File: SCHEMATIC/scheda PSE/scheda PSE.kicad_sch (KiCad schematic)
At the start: 4 parts

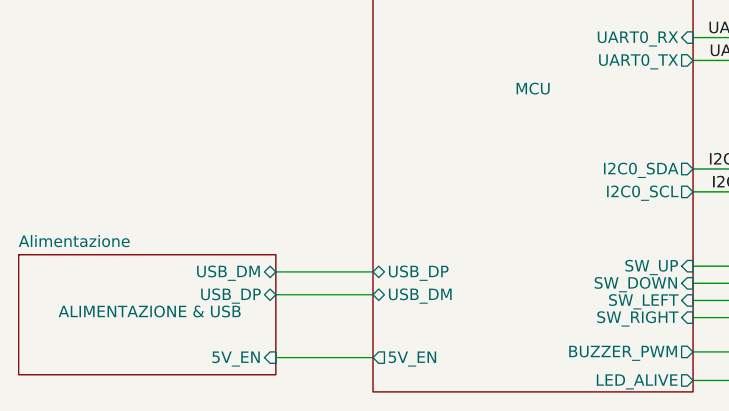
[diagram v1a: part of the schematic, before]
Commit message: iniziato lo broglio. Prima di continuare modificare pin schema
iniziato lo sbroglio della scheda, prima di continuare bisogna sistemare i pin che siano concordi con quelli degli altro (ovvero sistemarli come da tabella su telegram)
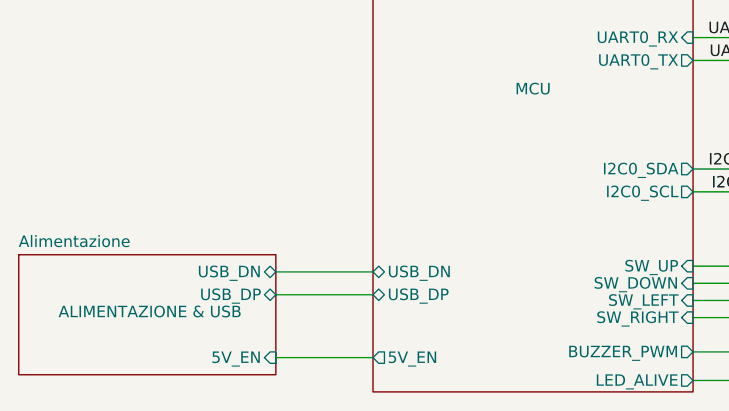
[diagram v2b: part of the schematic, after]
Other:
- sheet Alimentazione ports: added USB_DN; removed USB_DM
- sheet RP2040 ports: added USB_DN; removed USB_DM

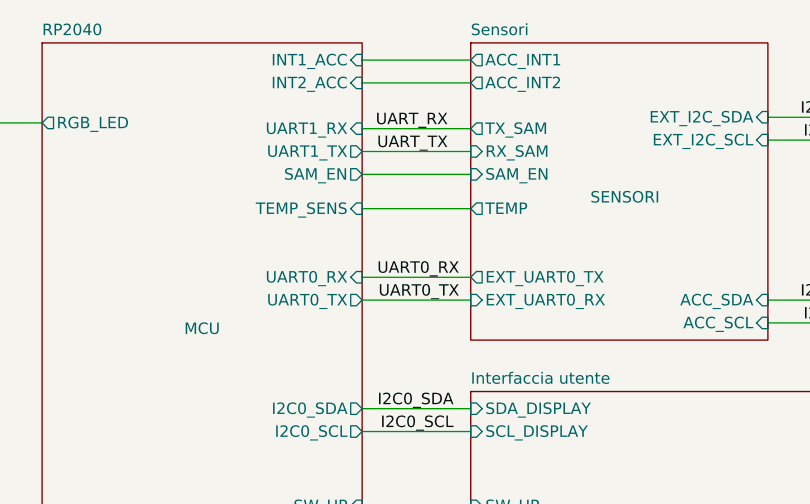
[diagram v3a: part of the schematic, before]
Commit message: modificato pin 2,3,14,15,16,17,18,27,28,29,30,31,32
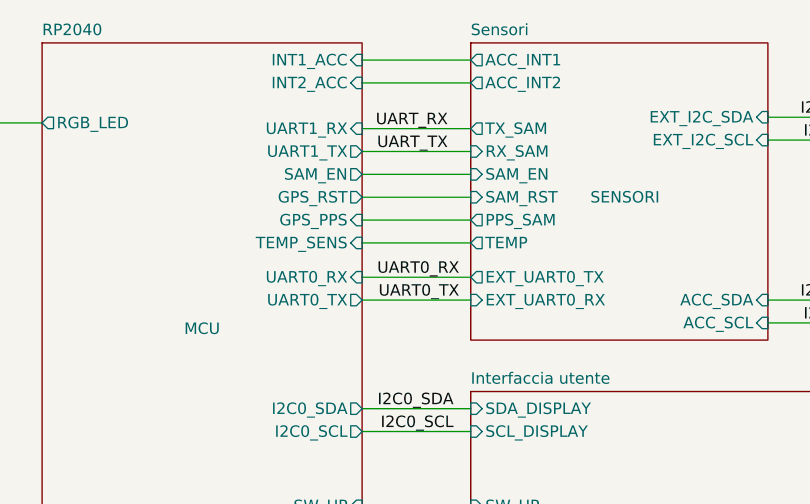
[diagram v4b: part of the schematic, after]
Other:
- sheet RP2040 ports: added GPS_PPS, GPS_RST; removed none
- sheet Sensori ports: added PPS_SAM, SAM_RST; removed none
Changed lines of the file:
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@@
+    (stroke (width 0) (type default) (color 0 0 0 0))
+  )
+  (wire (pts (xy 149.86 85.09) (xy 161.925 85.09))
     (stroke (width 0) (type default) (color 0 0 0 0))
   )
@@
     (stroke (width 0) (type default) (color 0 0 0 0))
   )
+  (wire (pts (xy 149.86 82.55) (xy 161.925 82.55))
+    (stroke (width 0) (type default) (color 0 0 0 0))
+  )
   (wire (pts (xy 149.86 106.045) (xy 161.925 106.045))
     (stroke (width 0) (type default) (color 0 0 0 0))
@@
     (stroke (width 0) (type default) (color 0 0 0 0))
   )
-  (wire (pts (xy 149.86 83.82) (xy 161.925 83.82))
+  (wire (pts (xy 149.86 87.63) (xy 161.925 87.63))
     (stroke (width 0) (type default) (color 0 0 0 0))
   )
@@
       (effects (font (size 1.27 1.27)) (justify left))
     )
-    (pin "TEMP" output (at 161.925 83.82 180)
+    (pin "TEMP" output (at 161.925 87.63 180)
       (effects (font (size 1.27 1.27)) (justify left))
     )
@@
     )
     (pin "EXT_UART0_TX" output (at 161.925 91.44 180)
+      (effects (font (size 1.27 1.27)) (justify left))
+    )
+    (pin "SAM_RST" input (at 161.925 82.55 180)
+      (effects (font (size 1.27 1.27)) (justify left))
+    )
+    (pin "PPS_SAM" output (at 161.925 85.09 180)
       (effects (font (size 1.27 1.27)) (justify left))
     )
@@
       (effects (font (size 1.27 1.27)) (justify right))
     )
-    (pin "TEMP_SENS" input (at 149.86 83.82 0)
+    (pin "TEMP_SENS" input (at 149.86 87.63 0)
       (effects (font (size 1.27 1.27)) (justify right))
     )
@@
       (effects (font (size 1.27 1.27)) (justify right))
     )
+    (pin "GPS_RST" output (at 149.86 82.55 0)
+      (effects (font (size 1.27 1.27)) (justify right))
+    )
+    (pin "GPS_PPS" input (at 149.86 85.09 0)
+      (effects (font (size 1.27 1.27)) (justify right))
+    )

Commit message: finito lo sbroglio (magari da ricontrollare)
finito lo sbroglio, controllato già io ma meglio ridare una controllata.
Da sistemare tutta la serigrafia
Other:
- sheet RP2040 ports: added ACC_SA0, GPS_EN; removed SAM_EN
- sheet Sensori ports: added ACC_SA0, SAM_PPS; removed PPS_SAM
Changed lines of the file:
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@@
     (stroke (width 0) (type default) (color 0 0 0 0))
   )
-  (wire (pts (xy 149.86 69.85) (xy 161.925 69.85))
+  (wire (pts (xy 149.86 66.675) (xy 161.925 66.675))
     (stroke (width 0) (type default) (color 0 0 0 0))
   )
@@
     (stroke (width 0) (type default) (color 0 0 0 0))
   )
+  (wire (pts (xy 149.86 69.215) (xy 161.925 69.215))
+    (stroke (width 0) (type default) (color 0 0 0 0))
+  )
   (wire (pts (xy 149.86 106.045) (xy 161.925 106.045))
     (stroke (width 0) (type default) (color 0 0 0 0))
@@
     (stroke (width 0) (type default) (color 0 0 0 0))
   )
-  (wire (pts (xy 149.86 67.31) (xy 161.925 67.31))
+  (wire (pts (xy 149.86 64.135) (xy 161.925 64.135))
     (stroke (width 0) (type default) (color 0 0 0 0))
   )
@@
     )
   )
-  (sheet (at 161.925 65.405) (size 33.02 33.02)
+  (sheet (at 161.925 62.23) (size 33.02 36.195)
     (stroke (width 0.1524) (type solid) (color 0 0 0 0))
     (fill (color 0 0 0 0.0000))
-    (property "Sheet name" "Sensori" (id 0) (at 161.925 64.6934 0)
+    (property "Sheet name" "Sensori" (id 0) (at 161.925 61.5184 0)
       (effects (font (size 1.27 1.27)) (justify left bottom))
     )
-    (property "Sheet file" "sensori.kicad_sch" (id 1) (at 161.925 92.71 0)
+    (property "Sheet file" "sensori.kicad_sch" (id 1) (at 161.925 89.535 0)
       (effects (font (size 1.27 1.27)) (justify left top) hide)
     )
-    (property "Etichetta" "SENSORI" (id 2) (at 179.07 82.55 0))
+    (property "Etichetta" "SENSORI" (id 2) (at 179.07 79.375 0))
     (pin "TX_SAM" output (at 161.925 74.93 180)
       (effects (font (size 1.27 1.27)) (justify left))
@@
       (effects (font (size 1.27 1.27)) (justify left))
     )
-    (pin "ACC_INT2" output (at 161.925 69.85 180)
-      (effects (font (size 1.27 1.27)) (justify left))
-    )
-    (pin "ACC_INT1" output (at 161.925 67.31 180)
+    (pin "ACC_INT2" output (at 161.925 66.675 180)
+      (effects (font (size 1.27 1.27)) (justify left))
+    )
+    (pin "ACC_INT1" output (at 161.925 64.135 180)
       (effects (font (size 1.27 1.27)) (justify left))
     )
@@
       (effects (font (size 1.27 1.27)) (justify left))
     )
-    (pin "PPS_SAM" output (at 161.925 85.09 180)
+    (pin "SAM_PPS" output (at 161.925 85.09 180)
+      (effects (font (size 1.27 1.27)) (justify left))
+    )
+    (pin "ACC_SA0" input (at 161.925 69.215 180)
       (effects (font (size 1.27 1.27)) (justify left))
     )
@@
     )
   )
-  (sheet (at 114.3 65.405) (size 35.56 65.405)
+  (sheet (at 114.3 62.23) (size 35.56 68.58)
     (stroke (width 0.1524) (type solid) (color 0 0 0 0))
     (fill (color 0 0 0 0.0000))
-    (property "Sheet name" "RP2040" (id 0) (at 114.3 64.6934 0)
+    (property "Sheet name" "RP2040" (id 0) (at 114.3 61.5184 0)
       (effects (font (size 1.27 1.27)) (justify left bottom))
     )
-    (property "Sheet file" "rp2040.kicad_sch" (id 1) (at 114.3 131.3946 0)
+    (property "Sheet file" "rp2040.kicad_sch" (id 1) (at 114.3 128.2196 0)
       (effects (font (size 1.27 1.27)) (justify left top) hide)
     )
-    (property "Etichetta" "MCU" (id 2) (at 132.08 97.155 0))
+    (property "Etichetta" "MCU" (id 2) (at 132.08 93.98 0))
     (pin "USB_DN" bidirectional (at 114.3 117.475 180)
       (effects (font (size 1.27 1.27)) (justify left))
@@
       (effects (font (size 1.27 1.27)) (justify left))
     )
-    (pin "INT1_ACC" input (at 149.86 67.31 0)
-      (effects (font (size 1.27 1.27)) (justify right))
-    )
-    (pin "INT2_ACC" input (at 149.86 69.85 0)
+    (pin "INT1_ACC" input (at 149.86 64.135 0)
+      (effects (font (size 1.27 1.27)) (justify right))
+    )
+    (pin "INT2_ACC" input (at 149.86 66.675 0)
       (effects (font (size 1.27 1.27)) (justify right))
     )
@@
       (effects (font (size 1.27 1.27)) (justify right))
     )
-    (pin "SAM_EN" output (at 149.86 80.01 0)
-      (effects (font (size 1.27 1.27)) (justify right))
-    )
     (pin "GPS_RST" output (at 149.86 82.55 0)
       (effects (font (size 1.27 1.27)) (justify right))
     )
     (pin "GPS_PPS" input (at 149.86 85.09 0)
+      (effects (font (size 1.27 1.27)) (justify right))
+    )
+    (pin "ACC_SA0" output (at 149.86 69.215 0)
+      (effects (font (size 1.27 1.27)) (justify right))
+    )
+    (pin "GPS_EN" output (at 149.86 80.01 0)
       (effects (font (size 1.27 1.27)) (justify right))
     )
@@
       (reference "#PWR078") (unit 1) (value "GND") (footprint "")
     )
-    (path "/7389e30f-cc4a-4964-bca3-cd95052ca62a/028caaaa-a788-48f0-8e29-0eb2d6869e1a"
-      (reference "#PWR079") (unit 1) (value "GND") (footprint "")
-    )
     (path "/7389e30f-cc4a-4964-bca3-cd95052ca62a/aa1b72ec-e86b-4492-ab96-18057e24a375"

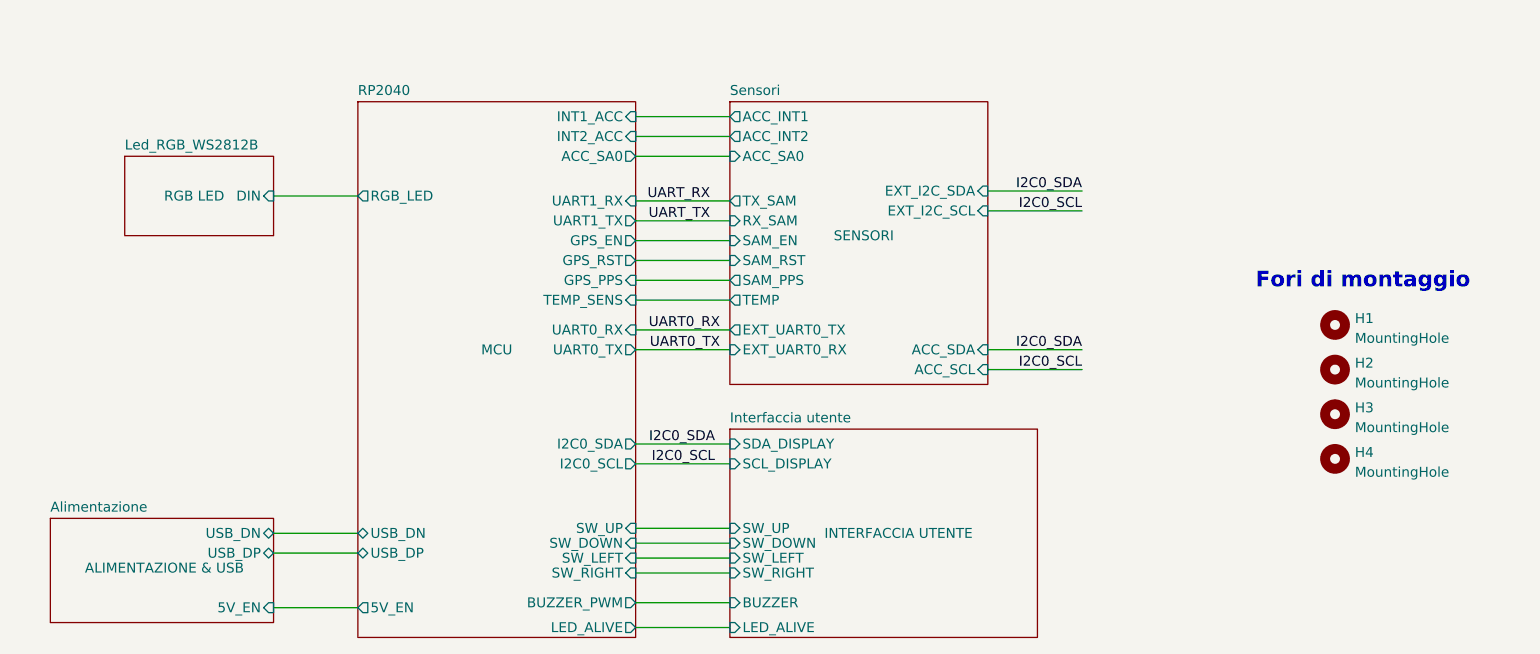
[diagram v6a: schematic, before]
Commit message: Aggiunte tutte le cose richieste dal prof
Aggiunte tutte le cose richieste dal prof:
wifi
servo
uscita led
MANCA DA METERE IL SOLDER MASK SUI PAD NON USATI DEL GPS
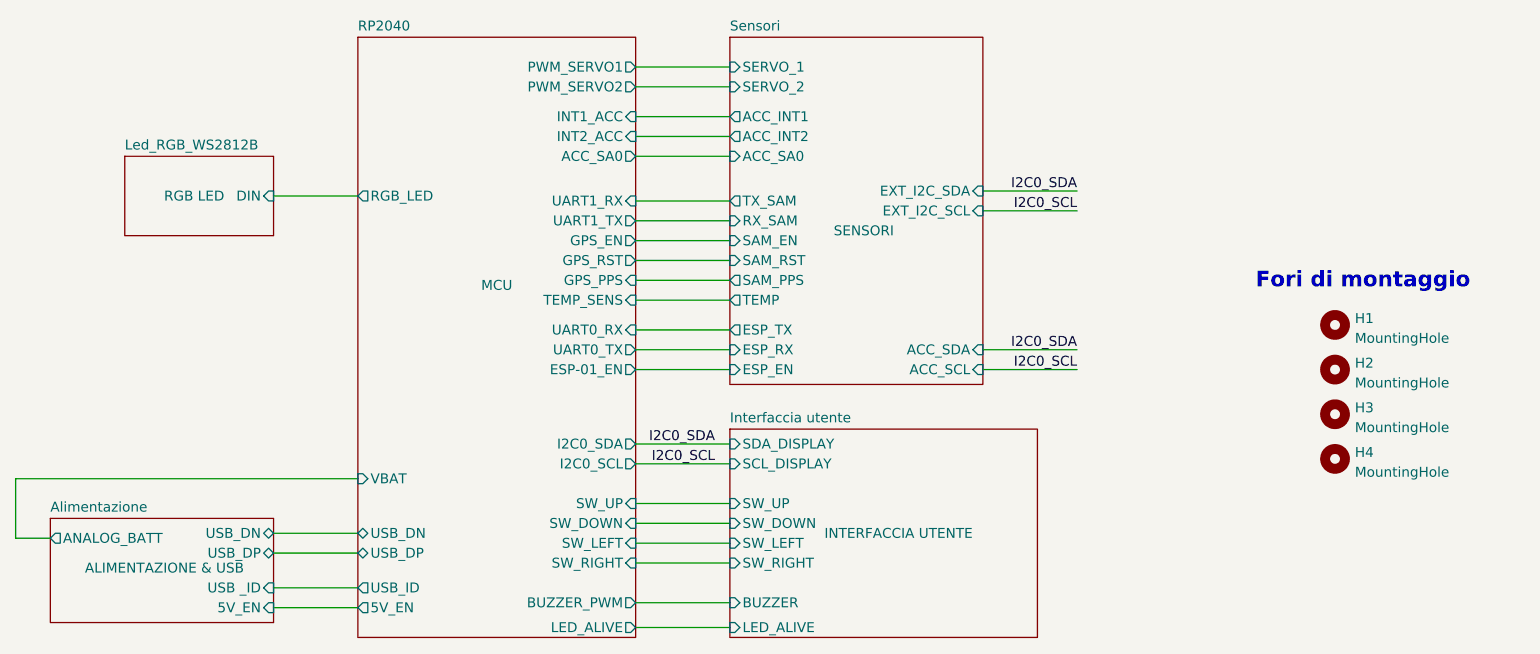
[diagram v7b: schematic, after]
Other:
- sheet Alimentazione ports: added ANALOG_BATT, USB _ID; removed none
- sheet RP2040 ports: added ESP-01_EN, PWM_SERVO1, PWM_SERVO2, USB_ID, VBAT; removed none
- sheet Sensori ports: added ESP_EN, ESP_RX, ESP_TX, SERVO_1, SERVO_2; removed EXT_UART0_RX, EXT_UART0_TX
